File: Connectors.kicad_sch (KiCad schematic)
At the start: 13 parts, among them J4 Conn_01x06, J5 Conn_01x06, U10 TJA1051T/3

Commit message: save
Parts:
- removed C28: 100n, Capacitor_SMD:C_0402_1005Metric, symbol Device:C_Small
- removed J4, J5: Conn_01x06, Connector_PinHeader_2.54mm:PinHeader_1x06_P2.54mm_Vertical, symbol Connector_Generic:Conn_01x06
- removed R20, R21: 22, Resistor_SMD:R_0402_1005Metric, symbol Device:R_Small
- added CAN1, GPS_Mag1, GPS_Serial1: SM04B-GHS-TB, CONN_SM04B-GHS-TB_JST, symbol SM04B-GHS-TB:SM04B-GHS-TB
- added J6: Conn_02x03_Odd_Even, Connector_IDC:IDC-Header_2x03_P2.54mm_Vertical, symbol Connector_Generic:Conn_02x03_Odd_Even
- added TELE1: SM06B-GHS-TB, CONN_SM06B-GHS-TB_JST, symbol SM06B-GHS-TB:SM06B-GHS-TB
- renumbered C29 to C27, C30 to C28, R15 to R14, R16 to R15, R17 to R16, R18 to R17, R19 to R18, U10 to U11
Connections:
- net +3.3V: now also J6.1 (Pin_1)
- net +5V: now also CAN1.4, GPS_Mag1.1, GPS_Serial1.1, TELE1.6
- net GND: now also CAN1.1, CAN1.5, CAN1.6, GPS_Mag1.4, GPS_Mag1.5, GPS_Mag1.6, GPS_Serial1.4, GPS_Serial1.5, GPS_Serial1.6, J6.5 (Pin_5), TELE1.1, TELE1.7, TELE1.8
- net SWO: now also J6.6 (Pin_6)
- net at R16.2: now also J6.2 (Pin_2)
- net at R15.2: now also J6.4 (Pin_4)
- net at R14.2: now also J6.3 (Pin_3)
- net CAN2+ renamed CANH
- net CANH: now also CAN1.3
- net CAN2- renamed CANL
- net CANL: now also CAN1.2
- new net GPS_RX: GPS_Serial1.3
- new net GPS_SCL: GPS_Mag1.2
- new net GPS_SDA: GPS_Mag1.3
- new net GPS_TX: GPS_Serial1.2
- new net TELE_CTS: TELE1.3
- new net TELE_RTS: TELE1.2
- new net TELE_RX: TELE1.4
- new net TELE_TX: TELE1.5
- no-connect marks 1 -> 0
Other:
- note removed: "UART/TTL"
- moved on the sheet: R14, R15, R16

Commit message: update V2_RC1
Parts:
- removed GPS_Mag1: SM04B-GHS-TB, CONN_SM04B-GHS-TB_JST, symbol SM04B-GHS-TB:SM04B-GHS-TB
- added J6: Conn_02x03_Odd_Even, Connector_PinSocket_2.00mm:PinSocket_2x03_P2.00mm_Vertical, symbol Connector_Generic:Conn_02x03_Odd_Even
- CAN1, GPS_Serial1: footprint CONN_SM04B-GHS-TB_JST -> mylib:CONN_SM04B-GHS-TB_JST
- J5: renamed from J6; footprint Connector_IDC:IDC-Header_2x03_P2.54mm_Vertical -> Connector_PinSocket_2.00mm:PinSocket_2x03_P2.00mm_Vertical
- TELE1: footprint CONN_SM06B-GHS-TB_JST -> mylib:CONN_SM06B-GHS-TB_JST
- renumbered C27 to C30, C28 to C31, R14 to R16, R15 to R17, R16 to R18, R17 to R19, R18 to R20, U11 to U12
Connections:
- net +3.3V: now also J5.5 (Pin_5); no longer J5.1 (Pin_1)
- net +5V: now also CAN1.1; no longer CAN1.4
- net GND: now also CAN1.4, J5.1 (Pin_1), J6.2 (Pin_2), J6.4 (Pin_4), J6.6 (Pin_6); no longer CAN1.1, J5.5 (Pin_5)
- net SWO: now also J5.2 (Pin_2); no longer J5.6 (Pin_6)
- net TELE_CTS: now also TELE1.2; no longer TELE1.3
- net TELE_RTS: now also TELE1.3; no longer TELE1.2
- net TELE_RX: now also TELE1.5; no longer TELE1.4
- net TELE_TX: now also TELE1.4; no longer TELE1.5
- net at R18.2: now also J5.6 (Pin_6); no longer J5.2 (Pin_2)
- new net Tim8_2: J6.5 (Pin_5)
- new net Tim8_3: J6.3 (Pin_3)
- new net Tim8_4: J6.1 (Pin_1)
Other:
- moved on the sheet: R18

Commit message: update
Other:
- note added: "Additional Connectors"
- moved on the sheet: J6, TELE1
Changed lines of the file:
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@@
 	(generator_version "9.0")
 	(paper "A4")
+	(text "Additional Connectors\n"
+		(exclude_from_sim no)
+		(at 180.594 38.862 0)
+		(effects
+			(font
+				(size 2.4892 2.4892)
+				(thickness 0.4978)
+				(bold yes)
+			)
+			(justify left bottom)
+		)
+	)
 	(text "SWD"
 		(exclude_from_sim no)
@@
 	)
 	(junction
-		(at 260.35 82.55)
+		(at 266.7 66.04)
 		(diameter 0)
 		(color 0 0 0 0)
@@
 	)
 	(junction
-		(at 219.71 120.65)
+		(at 212.09 93.98)
 		(diameter 0)
 		(color 0 0 0 0)
@@
 	)
 	(junction
-		(at 219.71 123.19)
+		(at 212.09 96.52)
 		(diameter 0)
 		(color 0 0 0 0)
@@
 	(wire
 		(pts
-			(xy 260.35 82.55) (xy 260.35 87.63)
+			(xy 266.7 66.04) (xy 266.7 71.12)
 		)
 		(stroke
@@
 		)
 	)
+	(polyline
+		(pts
+			(xy 173.99 33.02) (xy 278.13 33.02)
+		)
+		(stroke
+			(width 0)
+			(type dash)
+		)
+	)
 	(wire
 		(pts
@@
 		)
 	)
+	(polyline
+		(pts
+			(xy 278.13 104.14) (xy 173.99 104.14)
+		)
+		(stroke
+			(width 0)
+			(type dash)
+		)
+	)
 	(wire
 		(pts
@@
 		)
 	)
+	(polyline
+		(pts
+			(xy 278.13 104.14) (xy 278.13 33.02)
+		)
+		(stroke
+			(width 0)
+			(type dash)
+		)
+	)
 	(wire
 		(pts
@@
 	(wire
 		(pts
-			(xy 219.71 123.19) (xy 219.71 125.73)
+			(xy 212.09 96.52) (xy 212.09 99.06)
 		)
 		(stroke
@@
 		)
 	)
+	(polyline
+		(pts
+			(xy 173.99 104.14) (xy 173.99 34.2899)
+		)
+		(stroke
+			(width 0)
+			(type dash)
+		)
+	)
 	(wire
 		(pts
@@
 	(wire
 		(pts
-			(xy 219.71 120.65) (xy 219.71 123.19)
+			(xy 212.09 93.98) (xy 212.09 96.52)
 		)
 		(stroke
@@
 	(global_label "Tim8_4"
 		(shape input)
-		(at 207.01 120.65 180)
+		(at 199.39 93.98 180)
 		(effects
 			(font
@@
 		)
 		(property "Intersheetrefs" "${INTERSHEET_REFS}"
-			(at 207.01 120.65 0)
+			(at 199.39 93.98 0)
 			(effects
 				(font
@@
 	(global_label "TELE_CTS"
 		(shape input)
-		(at 242.57 81.28 180)
+		(at 248.92 64.77 180)
 		(effects
 			(font
@@
 		)
 		(property "Intersheetrefs" "${INTERSHEET_REFS}"
-			(at 242.57 81.28 0)
+			(at 248.92 64.77 0)
 			(effects
 				(font
@@
 	(global_label "TELE_RX"
 		(shape input)
-		(at 242.57 88.9 180)
+		(at 248.92 72.39 180)
 		(effects
 			(font
@@
 		)
 		(property "Intersheetrefs" "${INTERSHEET_REFS}"
-			(at 242.57 88.9 0)
+			(at 248.92 72.39 0)
 			(effects
 				(font
@@
 	(global_label "TELE_TX"
 		(shape input)
-		(at 242.57 86.36 180)
+		(at 248.92 69.85 180)
 		(effects
 			(font
@@
 		)
 		(property "Intersheetrefs" "${INTERSHEET_REFS}"
-			(at 242.57 86.36 0)
+			(at 248.92 69.85 0)
 			(effects
 				(font
@@
 	(global_label "TELE_RTS"
 		(shape input)
-		(at 242.57 83.82 180)
+		(at 248.92 67.31 180)
 		(effects
 			(font
@@
 		)
 		(property "Intersheetrefs" "${INTERSHEET_REFS}"
-			(at 242.57 83.82 0)
+			(at 248.92 67.31 0)
 			(effects
 				(font
@@
 	(global_label "Tim8_2"
 		(shape input)
-		(at 207.01 125.73 180)
+		(at 199.39 99.06 180)
 		(effects
 			(font
@@
 		)
 		(property "Intersheetrefs" "${INTERSHEET_REFS}"
-			(at 207.01 125.73 0)
+			(at 199.39 99.06 0)
 			(effects
 				(font
@@
 	(global_label "Tim8_3"
 		(shape input)
-		(at 207.01 123.19 180)
+		(at 199.39 96.52 180)
 		(effects
 			(font
@@
 		)
 		(property "Intersheetrefs" "${INTERSHEET_REFS}"
-			(at 207.01 123.19 0)
+			(at 199.39 96.52 0)
 			(effects
 				(font
@@
 	(symbol
 		(lib_id "power:GND")
-		(at 242.57 78.74 180)
+		(at 248.92 62.23 180)
 		(unit 1)
 		(exclude_from_sim no)
@@
 		(dnp no)
 		(property "Reference" "#PWR096"
-			(at 242.57 72.39 0)
+			(at 248.92 55.88 0)
 			(effects
 				(font
@@
 		)
 		(property "Value" "GND"
-			(at 242.443 74.3458 0)
+			(at 248.793 57.8358 0)
 			(effects
 				(font
@@
 		)
 		(property "Footprint" ""
-			(at 242.57 78.74 0)
+			(at 248.92 62.23 0)
 			(effects
 				(font
@@
 		)
 		(property "Datasheet" ""
-			(at 242.57 78.74 0)
+			(at 248.92 62.23 0)
 			(effects
 				(font
@@
 		)
 		(property "Description" "Power symbol creates a global label with name \"GND\" , ground"
-			(at 242.57 78.74 0)
+			(at 248.92 62.23 0)
 			(effects
 				(font
@@
 	(symbol
 		(lib_id "power:+5V")
-		(at 242.57 91.44 180)
+		(at 248.92 74.93 180)
 		(unit 1)
 		(exclude_from_sim no)
@@
 		(dnp no)
 		(property "Reference" "#PWR097"
-			(at 242.57 87.63 0)
+			(at 248.92 71.12 0)
 			(effects
 				(font
@@
 		)
 		(property "Value" "+5V"
-			(at 246.126 95.25 0)
+			(at 252.476 78.74 0)
 			(effects
 				(font
@@
 		)
 		(property "Footprint" ""
-			(at 242.57 91.44 0)
+			(at 248.92 74.93 0)
 			(effects
 				(font
@@
 		)
 		(property "Datasheet" ""
-			(at 242.57 91.44 0)
+			(at 248.92 74.93 0)
 			(effects
 				(font
@@
 		)
 		(property "Description" "Power symbol creates a global label with name \"+5V\""
-			(at 242.57 91.44 0)
+			(at 248.92 74.93 0)
 			(effects
 				(font
@@
 	(symbol
 		(lib_id "power:GND")
-		(at 260.35 82.55 90)
+		(at 266.7 66.04 90)
 		(unit 1)
 		(exclude_from_sim no)
@@
 		(dnp no)
 		(property "Reference" "#PWR098"
-			(at 266.7 82.55 0)
+			(at 273.05 66.04 0)
 			(effects
 				(font
@@
 		)
 		(property "Value" "GND"
-			(at 264.7442 82.423 0)
+			(at 271.0942 65.913 0)
 			(effects
 				(font
@@
 		)
 		(property "Footprint" ""
-			(at 260.35 82.55 0)
+			(at 266.7 66.04 0)
 			(effects
 				(font
@@
 		)
 		(property "Datasheet" ""
-			(at 260.35 82.55 0)
+			(at 266.7 66.04 0)
 			(effects
 				(font
@@
 		)
 		(property "Description" "Power symbol creates a global label with name \"GND\" , ground"
-			(at 260.35 82.55 0)
+			(at 266.7 66.04 0)
 			(effects
 				(font
@@
 	(symbol
 		(lib_id "SM06B-GHS-TB:SM06B-GHS-TB")
-		(at 242.57 78.74 0)
+		(at 248.92 62.23 0)
 		(unit 1)
 		(exclude_from_sim no)
@@
 		(dnp no)
 		(property "Reference" "TELE1"
-			(at 248.92 73.66 0)
+			(at 255.27 57.15 0)
 			(effects
 				(font
@@
 		)
 		(property "Value" "SM06B-GHS-TB"
-			(at 256.54 86.3599 0)
+			(at 262.89 69.8499 0)
 			(effects
 				(font
@@
 		)
 		(property "Footprint" "mylib:CONN_SM06B-GHS-TB_JST"
-			(at 242.57 78.74 0)
+			(at 248.92 62.23 0)
 			(effects
 				(font
@@
 		)
 		(property "Datasheet" "SM06B-GHS-TB"
-			(at 242.57 78.74 0)
+			(at 248.92 62.23 0)
 			(effects
 				(font
@@
 		)
 		(property "Description" ""
-			(at 242.57 78.74 0)
+			(at 248.92 62.23 0)
 			(effects
 				(font
@@
 	(symbol
 		(lib_id "power:GND")
-		(at 219.71 120.65 180)
+		(at 212.09 93.98 180)
 		(unit 1)
 		(exclude_from_sim no)
@@
 		(dnp no)
 		(property "Reference" "#PWR095"
-			(at 219.71 114.3 0)
+			(at 212.09 87.63 0)
 			(effects
 				(font
@@
 		)
 		(property "Value" "GND"
-			(at 219.583 116.2558 0)
+			(at 211.963 89.5858 0)
 			(effects
 				(font
@@
 		)
 		(property "Footprint" ""
-			(at 219.71 120.65 0)
+			(at 212.09 93.98 0)
 			(effects
 				(font
@@
 		)
 		(property "Datasheet" ""
-			(at 219.71 120.65 0)
+			(at 212.09 93.98 0)
 			(effects
 				(font
@@
 		)
 		(property "Description" "Power symbol creates a global label with name \"GND\" , ground"
-			(at 219.71 120.65 0)
+			(at 212.09 93.98 0)
 			(effects
 				(font
@@
 	(symbol
 		(lib_id "Connector_Generic:Conn_02x03_Odd_Even")
-		(at 212.09 123.19 0)
+		(at 204.47 96.52 0)
 		(unit 1)
 		(exclude_from_sim no)
@@
 		(dnp no)
 		(property "Reference" "J6"
-			(at 220.98 116.84 0)
+			(at 213.36 90.17 0)
 			(effects
 				(font
@@
 		)
 		(property "Value" "Conn_02x03_Odd_Even"
-			(at 213.36 116.84 0)
+			(at 205.74 90.17 0)
 			(effects
 				(font
@@
 		)
 		(property "Footprint" "Connector_PinSocket_2.00mm:PinSocket_2x03_P2.00mm_Vertical"
-			(at 212.09 123.19 0)
+			(at 204.47 96.52 0)
 			(effects
 				(font
@@
 		)
 		(property "Datasheet" "~"
-			(at 212.09 123.19 0)
+			(at 204.47 96.52 0)
 			(effects
 				(font
@@
 		)
 		(property "Description" "Generic connector, double row, 02x03, odd/even pin numbering scheme (row 1 odd numbers, row 2 even numbers), script generated (kicad-library-utils/schlib/autogen/connector/)"
-			(at 212.09 123.19 0)
-			(effects
-				(font
+			(at 204.47 96.52 0)
+			(effects
+				(font

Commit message: update
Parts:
- R19: LCSC Part (none) -> C166918
- R20: LCSC (none) -> C166918
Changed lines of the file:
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@@
 			)
 		)
-		(property "Description" "Resistor"
+		(property "Description" "Resistor RALEC RTT0360R0FTP"
+			(at 85.09 74.93 0)
+			(effects
+				(font
+					(size 1.27 1.27)
+				)
+				(hide yes)
+			)
+		)
+		(property "LCSC Part" "C166918"
 			(at 85.09 74.93 0)
 			(effects
@@
 			)
 		)
-		(property "Description" "Resistor"
+		(property "Description" "Resistor RTT0360R0FTP"
 			(at 95.25 74.93 0)
 			(effects
+				(font
+					(size 1.27 1.27)
+				)
+				(hide yes)
+			)
+		)
+		(property "LCSC" "C166918"
+			(at 95.25 74.93 0)
+			(effects

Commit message: PumbaaV2_RC2
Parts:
- CAN1, GPS_Serial1: value SM04B-GHS-TB -> SM04B-GHS-TB(LF)(SN)
- TELE1: value SM06B-GHS-TB -> SM06B-GHS-TB(LF)(SN)
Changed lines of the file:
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@@
 			)
 		)
-		(property "Value" "SM04B-GHS-TB"
+		(property "Value" "SM04B-GHS-TB(LF)(SN)"
 			(at 215.9 63.4999 0)
 			(effects
@@
 			)
 		)
-		(property "Value" "SM06B-GHS-TB"
+		(property "Value" "SM06B-GHS-TB(LF)(SN)"
 			(at 262.89 69.8499 0)
 			(effects
@@
 			)
 		)
-		(property "Value" "SM04B-GHS-TB"
+		(property "Value" "SM04B-GHS-TB(LF)(SN)"
 			(at 123.19 68.5799 0)
 			(effects

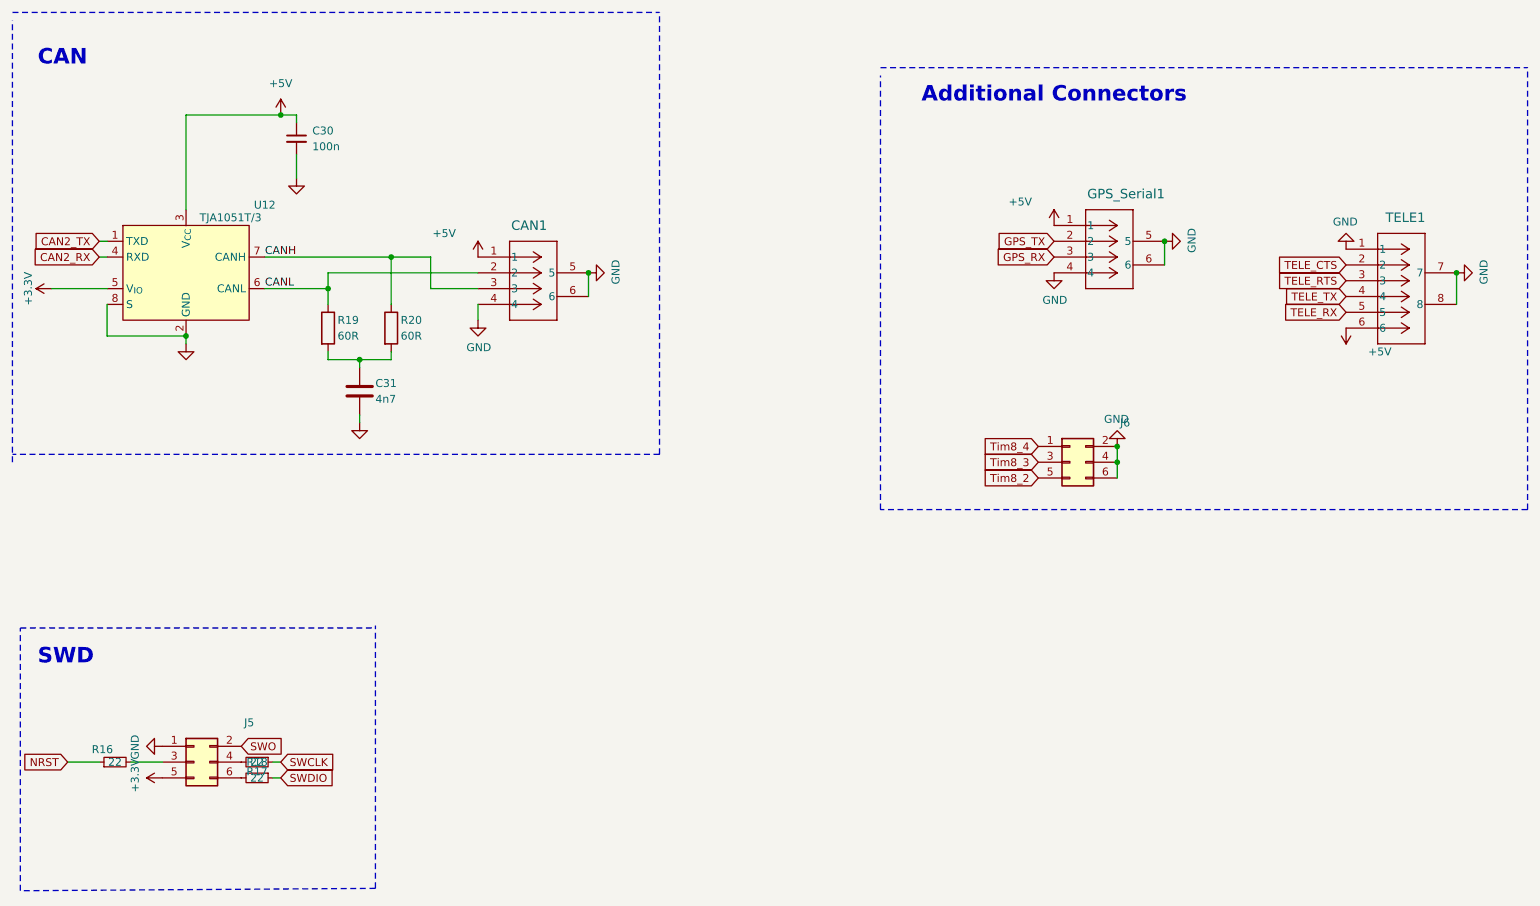
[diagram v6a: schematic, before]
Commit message: compact  IMU module for integration
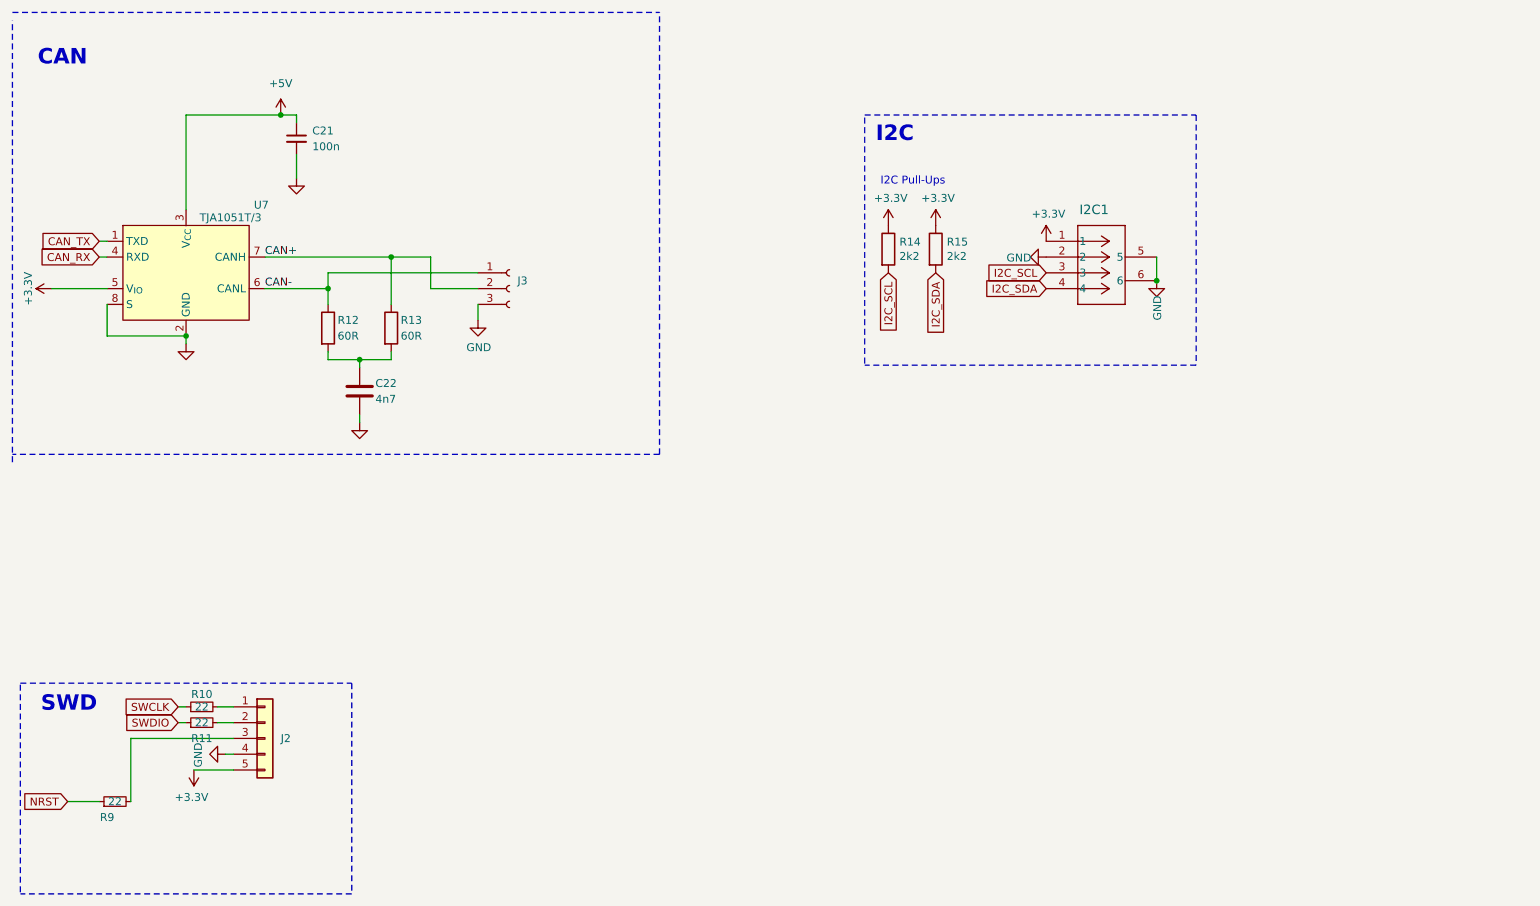
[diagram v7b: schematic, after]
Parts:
- removed CAN1, GPS_Serial1: SM04B-GHS-TB(LF)(SN), mylib:CONN_SM04B-GHS-TB_JST, symbol SM04B-GHS-TB:SM04B-GHS-TB
- removed J5, J6: Conn_02x03_Odd_Even, Connector_PinSocket_2.00mm:PinSocket_2x03_P2.00mm_Vertical, symbol Connector_Generic:Conn_02x03_Odd_Even
- removed TELE1: SM06B-GHS-TB(LF)(SN), mylib:CONN_SM06B-GHS-TB_JST, symbol SM06B-GHS-TB:SM06B-GHS-TB
- added I2C1: SM04B-GHS-TB(LF)(SN), mylib:CONN_SM04B-GHS-TB_JST, symbol SM04B-GHS-TB:SM04B-GHS-TB
- added J2: ZX-PZ2.54-1-5PZZ, Connector_PinHeader_2.54mm:PinHeader_1x05_P2.54mm_Vertical, symbol Connector_Generic:Conn_01x05
- added J3: Conn_01x03_Socket, Connector_PinHeader_2.54mm:PinHeader_1x03_P2.54mm_Vertical, symbol Connector:Conn_01x03_Socket
- added R14, R15: 2k2, Resistor_SMD:R_0402_1005Metric, symbol Device:R
- renumbered C30 to C21, C31 to C22, R17 to R10, R18 to R11, R19 to R12, R20 to R13, R16 to R9, U12 to U7
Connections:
- net +3.3V: now also I2C1.1, J2.5 (Pin_5), R14.1, R15.1
- net GND: now also I2C1.2, I2C1.5, I2C1.6, J2.4 (Pin_4), J3.3 (Pin_3)
- net at R11.2: now also J2.2 (Pin_2)
- net at R10.2: now also J2.1 (Pin_1)
- net at R9.2: now also J2.3 (Pin_3)
- net CAN2_RX renamed CAN_RX
- net CAN2_TX renamed CAN_TX
- net CANH renamed CAN+
- net CAN+: now also J3.2 (Pin_2)
- net CANL renamed CAN-
- net CAN-: now also J3.1 (Pin_1)
- new net I2C_SCL: I2C1.3, R14.2
- new net I2C_SDA: I2C1.4, R15.2
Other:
- note added: "I2C"
- note added: "I2C Pull-Ups"
- note removed: "Additional Connectors"
- moved on the sheet: R10, R11, R9
